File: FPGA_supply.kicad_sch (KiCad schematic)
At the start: 3 parts

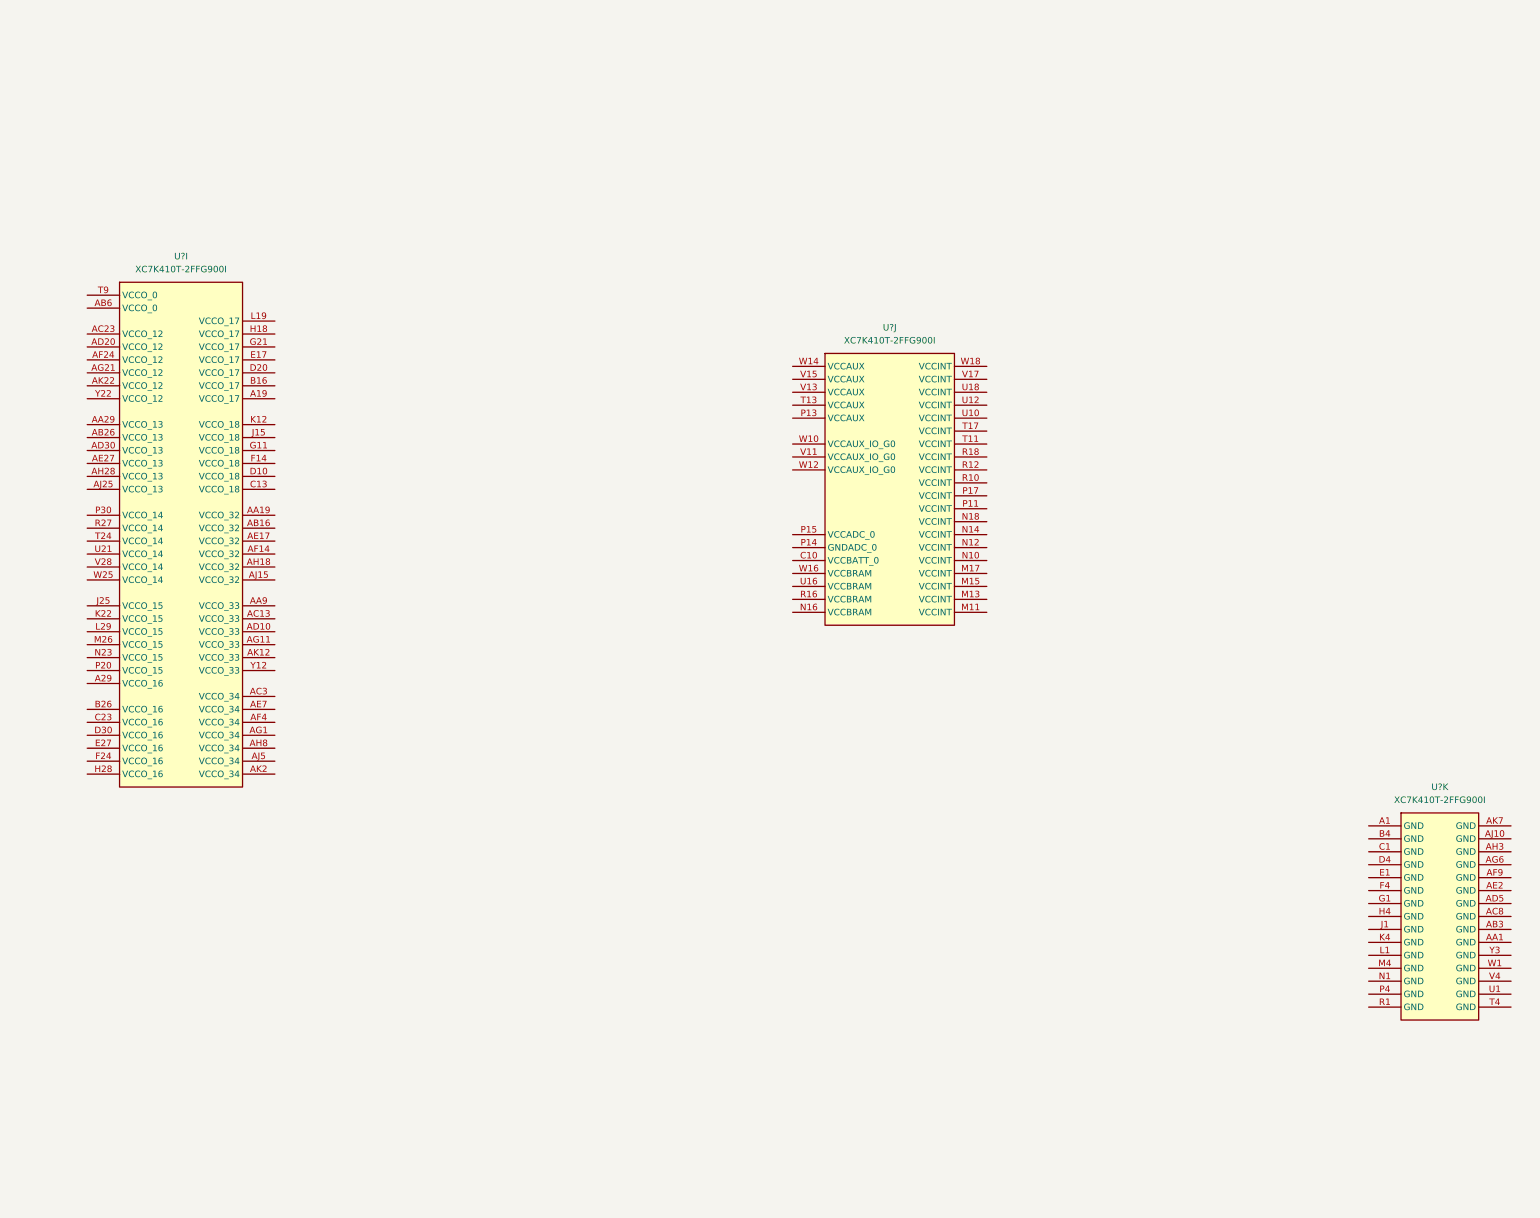
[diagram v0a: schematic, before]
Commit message: Add mandatory decoupling
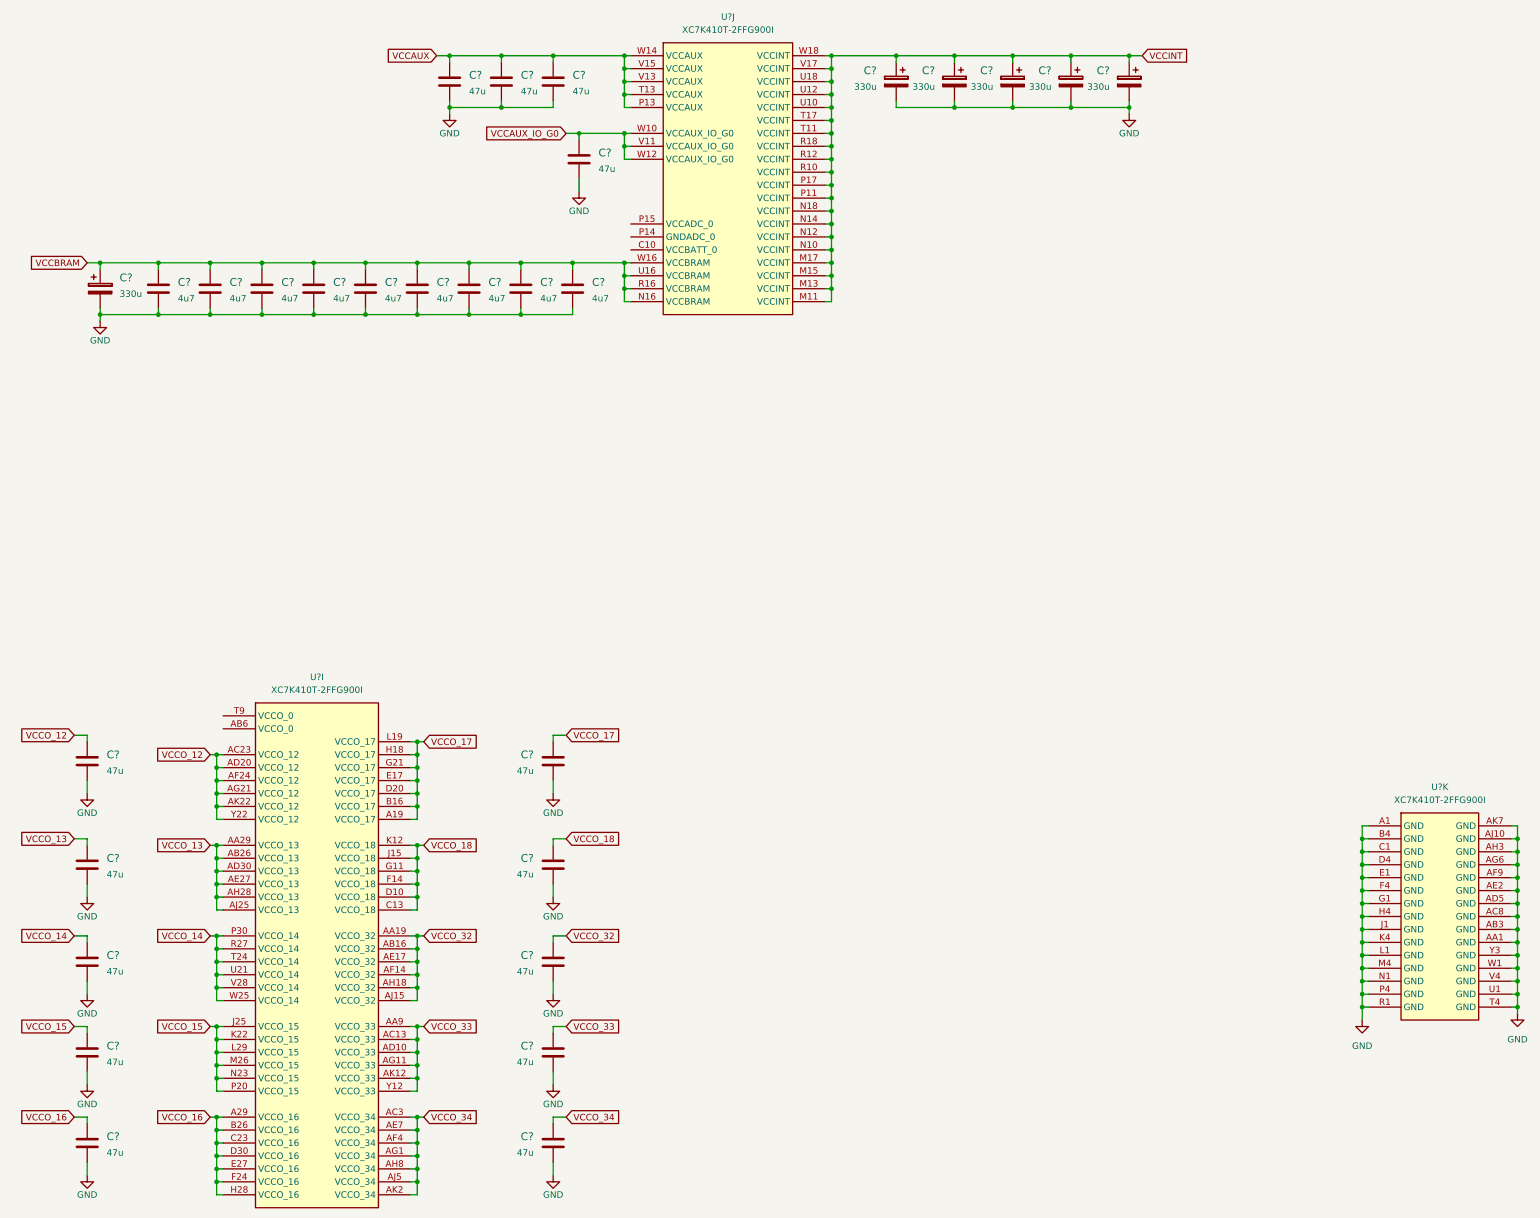
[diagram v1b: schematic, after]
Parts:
- added C? (x14): C_47u_0603, antmicro-footprints:0603-cap, symbol antmicroCapacitors0603:C_47u_0603
- added C? (x6): C_330u_KEMET_B, antmicro-footprints:KEMET_B, symbol antmicroCapacitorspol:C_330u_KEMET_B
- added C? (x9): C_4u7_0402, antmicro-footprints:0402-cap, symbol antmicroCapacitors0402:C_4u7_0402
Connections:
- net VCCO_17: now reaches U?.A19 (VCCO_17)
- net VCCO_17: now also U?.B16 (VCCO_17), U?.D20 (VCCO_17), U?.E17 (VCCO_17), U?.G21 (VCCO_17), U?.H18 (VCCO_17), U?.L19 (VCCO_17), C?.1
- net VCCO_16: now reaches U?.A29 (VCCO_16)
- net VCCO_16: now also U?.B26 (VCCO_16), U?.C23 (VCCO_16), U?.D30 (VCCO_16), U?.E27 (VCCO_16), U?.F24 (VCCO_16), U?.H28 (VCCO_16), C?.1
- net VCCO_32: now reaches U?.AA19 (VCCO_32)
- net VCCO_32: now also U?.AB16 (VCCO_32), U?.AE17 (VCCO_32), U?.AF14 (VCCO_32), U?.AH18 (VCCO_32), U?.AJ15 (VCCO_32), C?.1
- net VCCO_13: now reaches U?.AA29 (VCCO_13)
- net VCCO_13: now also U?.AB26 (VCCO_13), U?.AD30 (VCCO_13), U?.AE27 (VCCO_13), U?.AH28 (VCCO_13), U?.AJ25 (VCCO_13), C?.1
- net VCCO_33: now reaches U?.AA9 (VCCO_33)
- net VCCO_33: now also U?.AC13 (VCCO_33), U?.AD10 (VCCO_33), U?.AG11 (VCCO_33), U?.AK12 (VCCO_33), U?.Y12 (VCCO_33), C?.1
- net VCCO_12: now reaches U?.AC23 (VCCO_12)
- net VCCO_12: now also U?.AD20 (VCCO_12), U?.AF24 (VCCO_12), U?.AG21 (VCCO_12), U?.AK22 (VCCO_12), U?.Y22 (VCCO_12), C?.1
- net VCCO_34: now reaches U?.AC3 (VCCO_34)
- net VCCO_34: now also U?.AE7 (VCCO_34), U?.AF4 (VCCO_34), U?.AG1 (VCCO_34), U?.AH8 (VCCO_34), U?.AJ5 (VCCO_34), U?.AK2 (VCCO_34), C?.1
- net VCCO_18: now reaches U?.C13 (VCCO_18)
- net VCCO_18: now also U?.D10 (VCCO_18), U?.F14 (VCCO_18), U?.G11 (VCCO_18), U?.J15 (VCCO_18), U?.K12 (VCCO_18), C?.1
- net VCCO_15: now reaches U?.J25 (VCCO_15)
- net VCCO_15: now also U?.K22 (VCCO_15), U?.L29 (VCCO_15), U?.M26 (VCCO_15), U?.N23 (VCCO_15), U?.P20 (VCCO_15), C?.1
- net VCCO_14: now reaches U?.P30 (VCCO_14)
- net VCCO_14: now also U?.R27 (VCCO_14), U?.T24 (VCCO_14), U?.U21 (VCCO_14), U?.V28 (VCCO_14), U?.W25 (VCCO_14), C?.1
- net VCCINT: now reaches U?.M11 (VCCINT)
- net VCCINT: now also U?.M13 (VCCINT), U?.M15 (VCCINT), U?.M17 (VCCINT), U?.N10 (VCCINT), U?.N12 (VCCINT), U?.N14 (VCCINT), U?.N18 (VCCINT), U?.P11 (VCCINT), U?.P17 (VCCINT), U?.R10 (VCCINT), U?.R12 (VCCINT), U?.R18 (VCCINT), U?.T11 (VCCINT), U?.T17 (VCCINT), U?.U10 (VCCINT), U?.U12 (VCCINT), U?.U18 (VCCINT), U?.V17 (VCCINT), U?.W18 (VCCINT), C?.1, C?.1, C?.1, C?.1, C?.1
- net VCCBRAM: now reaches U?.N16 (VCCBRAM)
- net VCCBRAM: now also U?.R16 (VCCBRAM), U?.U16 (VCCBRAM), U?.W16 (VCCBRAM), C?.1, C?.1, C?.1, C?.1, C?.1, C?.1, C?.1, C?.1, C?.1, C?.1
- net VCCAUX: now reaches U?.P13 (VCCAUX)
- net VCCAUX: now also U?.T13 (VCCAUX), U?.V13 (VCCAUX), U?.V15 (VCCAUX), U?.W14 (VCCAUX), C?.1, C?.1, C?.1
- net VCCAUX_IO_G0: now reaches U?.V11 (VCCAUX_IO_G0)
- net VCCAUX_IO_G0: now also U?.W10 (VCCAUX_IO_G0), U?.W12 (VCCAUX_IO_G0), C?.1
- net GND: now reaches U?.A1 (GND), U?.A14 (GND), U?.A2 (GND), U?.A24 (GND), U?.A5 (GND), U?.A6 (GND), U?.A9 (GND)
- net GND: now also U?.AA1 (GND), U?.AA14 (GND), U?.AA2 (GND), U?.AA24 (GND), U?.AA5 (GND), U?.AA6 (GND), U?.AA7 (GND), U?.AB11 (GND), U?.AB21 (GND), U?.AB3 (GND), U?.AB4 (GND), U?.AC18 (GND), U?.AC28 (GND), U?.AC8 (GND), U?.AD15 (GND), U?.AD25 (GND), U?.AD5 (GND), U?.AE12 (GND), U?.AE2 (GND), U?.AE22 (GND), U?.AF19 (GND), U?.AF29 (GND), U?.AF9 (GND), U?.AG16 (GND), U?.AG26 (GND), U?.AG6 (GND), U?.AH13 (GND), U?.AH23 (GND), U?.AH3 (GND), U?.AJ10 (GND), U?.AJ20 (GND), U?.AJ30 (GND), U?.AK17 (GND), U?.AK27 (GND), U?.AK7 (GND), U?.B11 (GND), U?.B21 (GND), U?.B4 (GND), U?.B8 (GND), U?.B9 (GND), U?.C1 (GND), U?.C18 (GND), U?.C2 (GND), U?.C28 (GND), U?.C6 (GND), U?.C9 (GND), U?.D15 (GND), U?.D25 (GND), U?.D4 (GND), U?.D8 (GND), U?.D9 (GND), U?.E1 (GND), U?.E12 (GND), U?.E2 (GND), U?.E22 (GND), U?.E6 (GND), U?.E9 (GND), U?.F19 (GND), U?.F29 (GND), U?.F4 (GND), U?.F8 (GND), U?.F9 (GND), U?.G1 (GND), U?.G16 (GND), U?.G2 (GND), U?.G26 (GND), U?.G6 (GND), U?.G9 (GND), U?.H13 (GND), U?.H23 (GND), U?.H4 (GND), U?.H8 (GND), U?.H9 (GND), U?.J1 (GND), U?.J10 (GND), U?.J2 (GND), U?.J20 (GND), U?.J30 (GND), U?.J6 (GND), U?.J9 (GND), U?.K17 (GND), U?.K27 (GND), U?.K4 (GND), U?.K8 (GND), U?.K9 (GND), U?.L1 (GND), U?.L14 (GND), U?.L2 (GND), U?.L24 (GND), U?.L6 (GND), U?.L9 (GND), U?.M12 (GND), U?.M14 (GND), U?.M16 (GND), U?.M18 (GND), U?.M21 (GND), U?.M4 (GND), U?.M8 (GND), U?.M9 (GND), U?.N1 (GND), U?.N11 (GND), U?.N13 (GND), U?.N15 (GND), U?.N17 (GND), U?.N2 (GND), U?.N28 (GND), U?.N6 (GND), U?.N9 (GND), U?.P10 (GND), U?.P12 (GND), U?.P16 (GND), U?.P18 (GND), U?.P25 (GND), U?.P4 (GND), U?.P8 (GND), U?.P9 (GND), U?.R1 (GND), U?.R11 (GND), U?.R13 (GND), U?.R17 (GND), U?.R2 (GND), U?.R22 (GND), U?.R6 (GND), U?.R9 (GND), U?.T10 (GND), U?.T12 (GND), U?.T16 (GND), U?.T18 (GND), U?.T19 (GND), U?.T29 (GND), U?.T4 (GND), U?.T8 (GND), U?.U1 (GND), U?.U11 (GND), U?.U13 (GND), U?.U17 (GND), U?.U2 (GND), U?.U26 (GND), U?.U6 (GND), U?.U9 (GND), U?.V10 (GND), U?.V12 (GND), U?.V14 (GND), U?.V16 (GND), U?.V18 (GND), U?.V23 (GND), U?.V4 (GND), U?.V8 (GND), U?.V9 (GND), U?.W1 (GND), U?.W11 (GND), U?.W13 (GND), U?.W15 (GND), U?.W17 (GND), U?.W2 (GND), U?.W20 (GND), U?.W30 (GND), U?.W6 (GND), U?.W9 (GND), U?.Y17 (GND), U?.Y27 (GND), U?.Y3 (GND), U?.Y4 (GND), U?.Y7 (GND), U?.Y8 (GND), U?.Y9 (GND), C?.2, C?.2, C?.2, C?.2, C?.2, C?.2, C?.2, C?.2, C?.2, C?.2, C?.2, C?.2, C?.2, C?.2, C?.2, C?.2, C?.2, C?.2, C?.2, C?.2, C?.2, C?.2, C?.2, C?.2, C?.2, C?.2, C?.2, C?.2, C?.2
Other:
- moved on the sheet: U?I, U?J

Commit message: Add MT41K512M8DA DDR3L
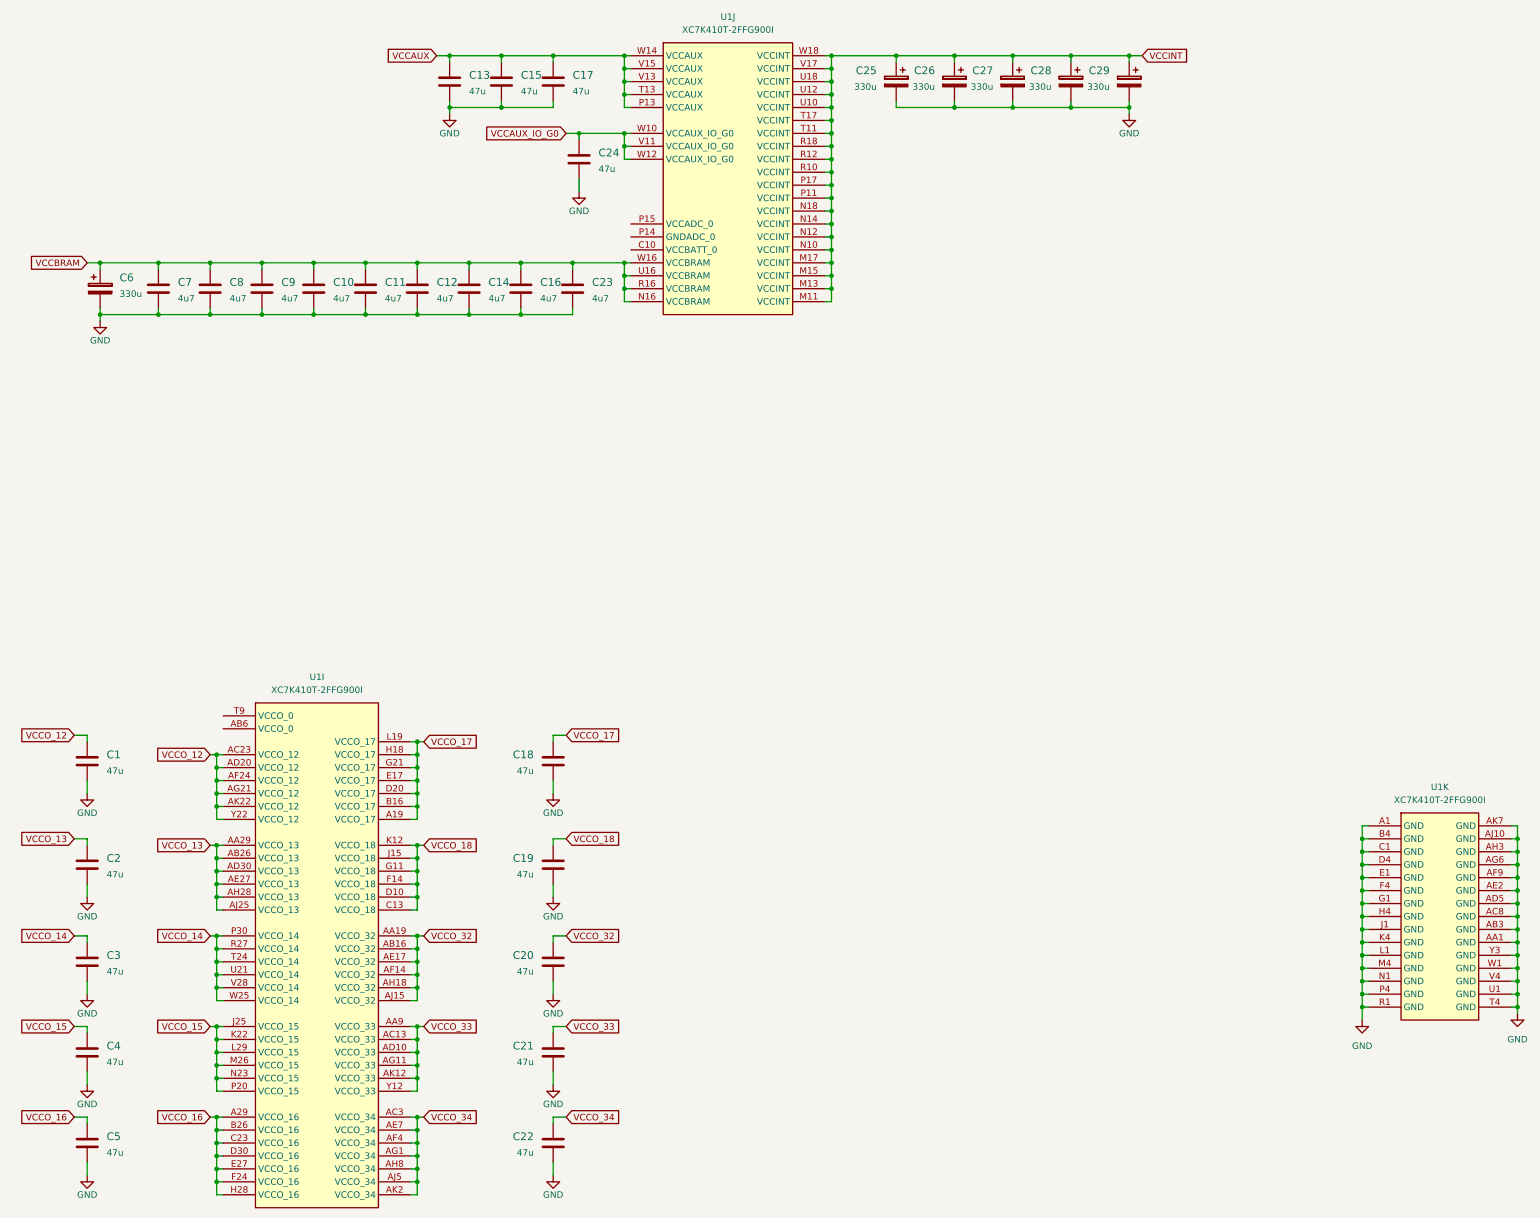
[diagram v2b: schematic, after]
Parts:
- gave numbers to parts that had none: 30

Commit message: Unify title block
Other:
- title: (none) -> K410T devboard
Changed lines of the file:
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@@
   (paper "A3")
   (title_block
-    (comment 1 "www.antmicro.com")
-    (comment 2 "Antmicro Ltd")
+    (title "K410T devboard")
+    (date "2022-12-20")
+    (rev "0.0.99")
   )
   (junction (at 123.19 269.24) (diameter 0) (color 0 0 0 0)
